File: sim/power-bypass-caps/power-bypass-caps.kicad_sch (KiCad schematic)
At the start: 248 parts

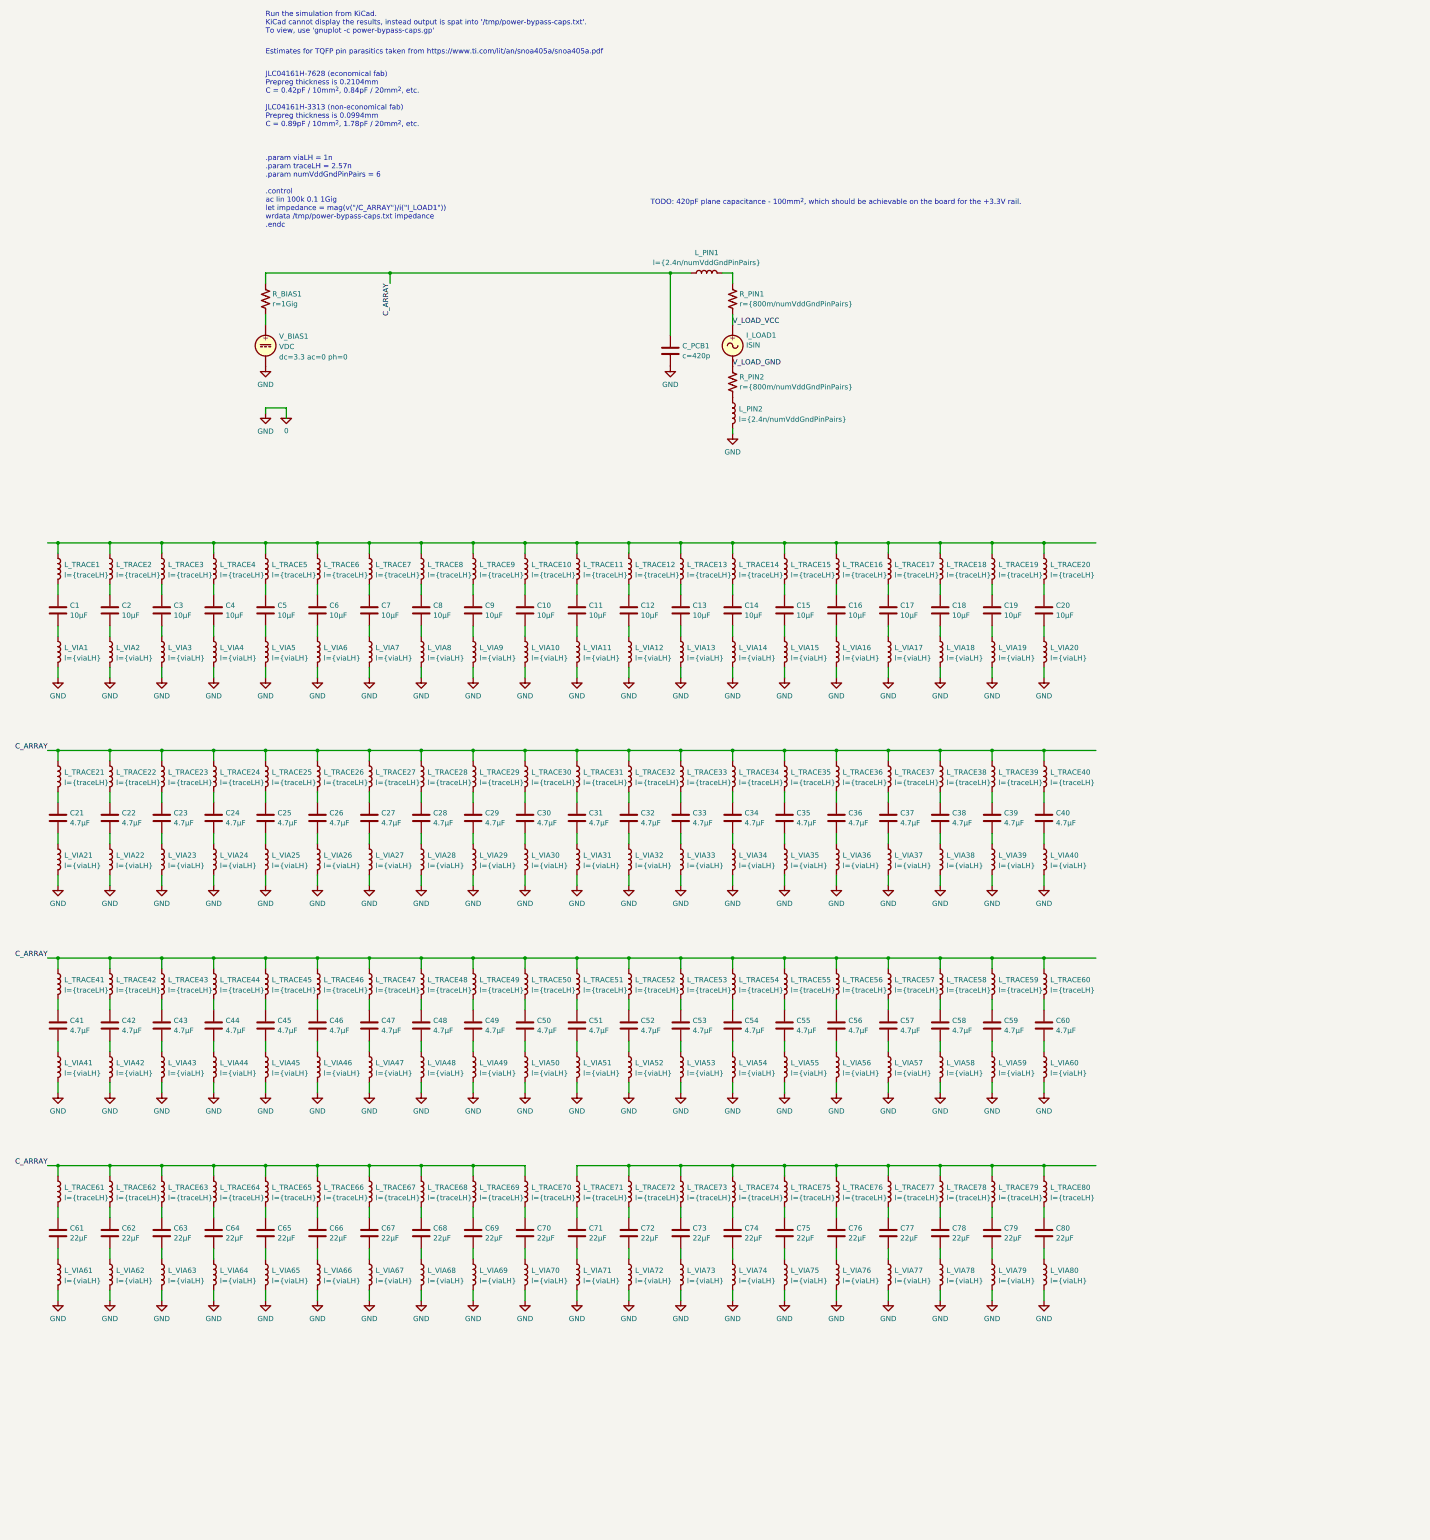
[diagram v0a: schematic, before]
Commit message: Some simulations around bypass capacitors.
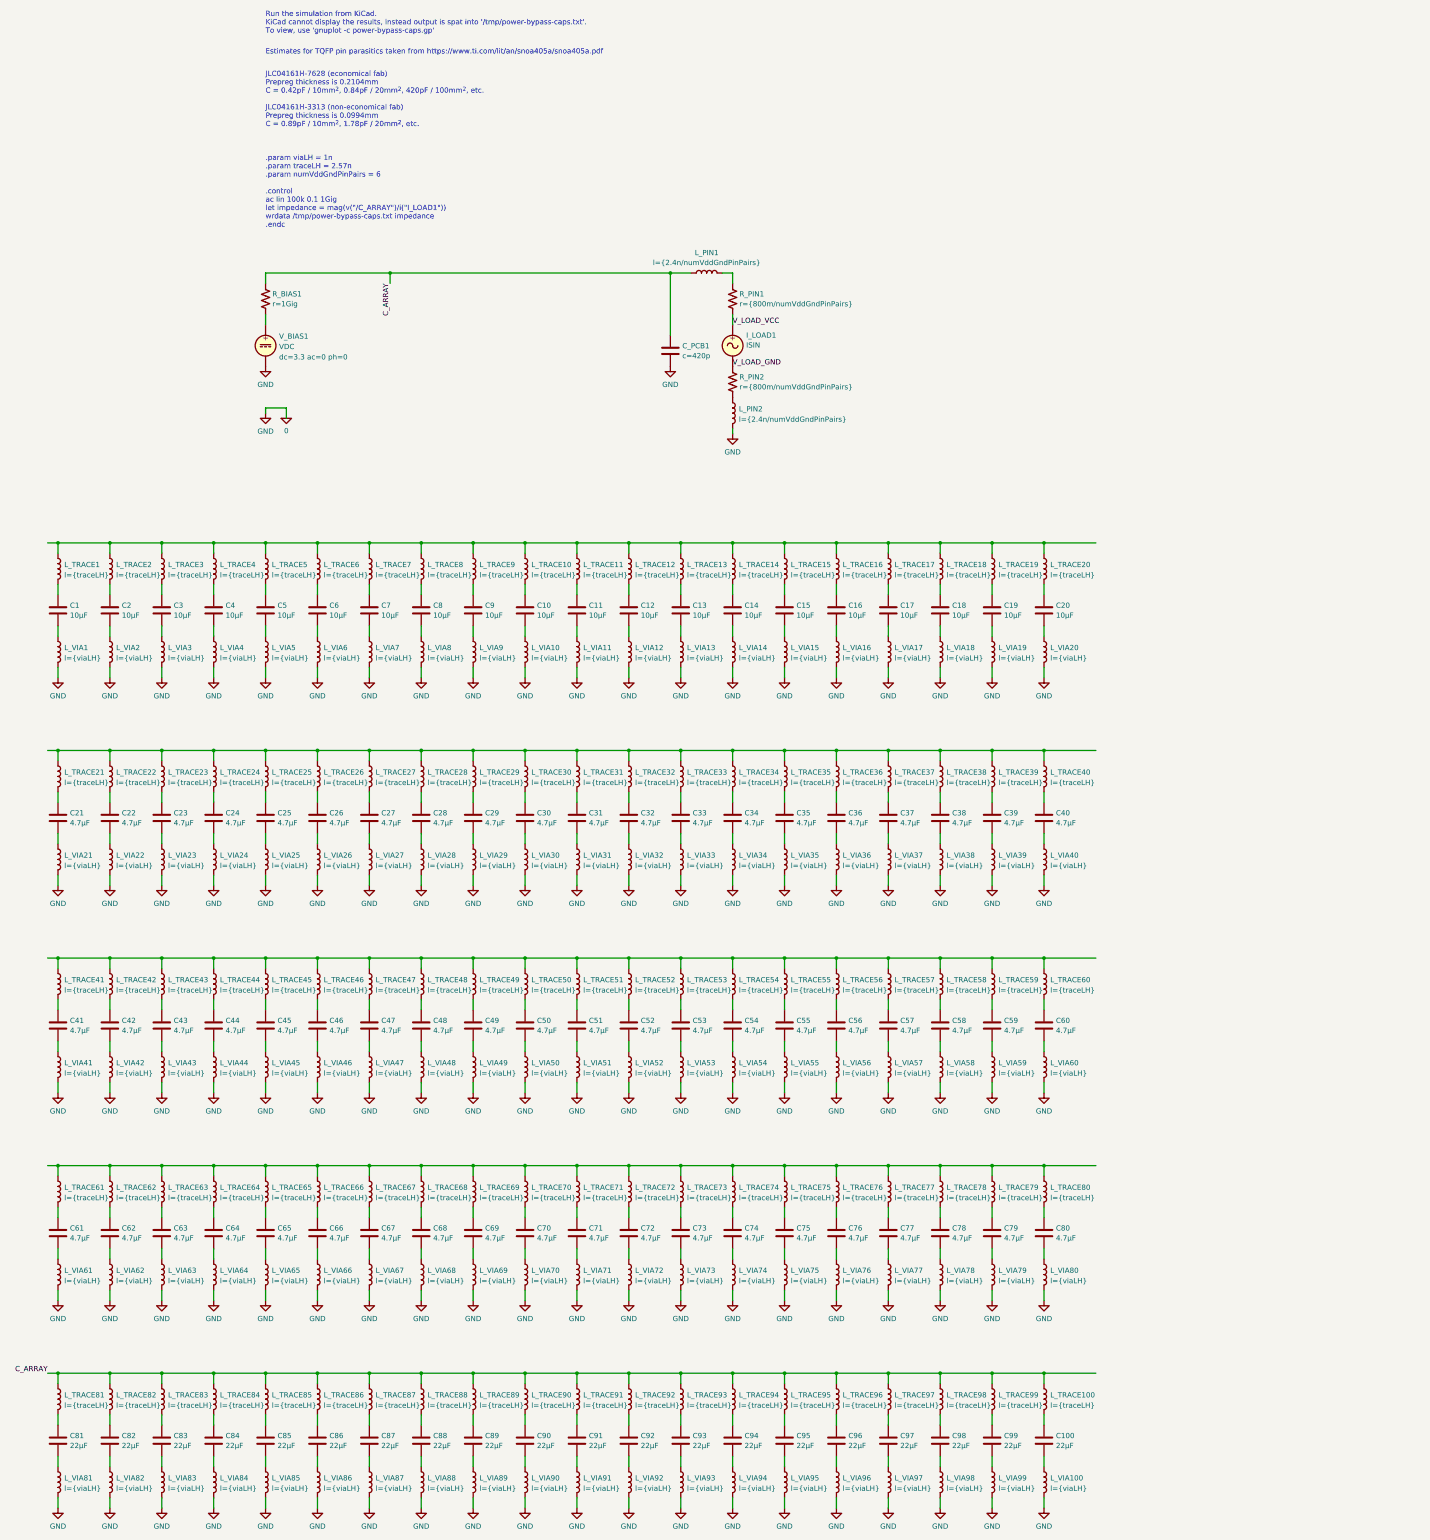
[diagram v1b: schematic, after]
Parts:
- added C100, C81, C82, C83, C84, C85, C86, C87, C88, C89, C90, C91, C92, C93, C94, C95, C96, C97, C98, C99: 22μF, restall-generic-capacitors:unpolarised-nominal-0402-1005, symbol restall-generic-capacitors:capacitor-unpolarised
- added L_TRACE100, L_TRACE81, L_TRACE82, L_TRACE83, L_TRACE84, L_TRACE85, L_TRACE86, L_TRACE87, L_TRACE88, L_TRACE89, L_TRACE90, L_TRACE91, L_TRACE92, L_TRACE93, L_TRACE94, L_TRACE95, L_TRACE96, L_TRACE97, L_TRACE98, L_TRACE99, L_VIA100, L_VIA81, L_VIA82, L_VIA83, L_VIA84, L_VIA85, L_VIA86, L_VIA87, L_VIA88, L_VIA89, L_VIA90, L_VIA91, L_VIA92, L_VIA93, L_VIA94, L_VIA95, L_VIA96, L_VIA97, L_VIA98, L_VIA99: ${SIM.PARAMS}, symbol restall-generic-inductors:l-air
- C61, C62, C63, C64, C65, C66, C67, C68, C69, C70, C71, C72, C73, C74, C75, C76, C77, C78, C79, C80: value 22μF -> 4.7μF
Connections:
- net 0: now also L_VIA100.2 (P2), L_VIA81.2 (P2), L_VIA82.2 (P2), L_VIA83.2 (P2), L_VIA84.2 (P2), L_VIA85.2 (P2), L_VIA86.2 (P2), L_VIA87.2 (P2), L_VIA88.2 (P2), L_VIA89.2 (P2), L_VIA90.2 (P2), L_VIA91.2 (P2), L_VIA92.2 (P2), L_VIA93.2 (P2), L_VIA94.2 (P2), L_VIA95.2 (P2), L_VIA96.2 (P2), L_VIA97.2 (P2), L_VIA98.2 (P2), L_VIA99.2 (P2)
- net C_ARRAY: now also L_TRACE100.1 (P1), L_TRACE81.1 (P1), L_TRACE82.1 (P1), L_TRACE83.1 (P1), L_TRACE84.1 (P1), L_TRACE85.1 (P1), L_TRACE86.1 (P1), L_TRACE87.1 (P1), L_TRACE88.1 (P1), L_TRACE89.1 (P1), L_TRACE90.1 (P1), L_TRACE91.1 (P1), L_TRACE92.1 (P1), L_TRACE93.1 (P1), L_TRACE94.1 (P1), L_TRACE95.1 (P1), L_TRACE96.1 (P1), L_TRACE97.1 (P1), L_TRACE98.1 (P1), L_TRACE99.1 (P1); no longer L_TRACE21.1 (P1), L_TRACE22.1 (P1), L_TRACE23.1 (P1), L_TRACE24.1 (P1), L_TRACE25.1 (P1), L_TRACE26.1 (P1), L_TRACE27.1 (P1), L_TRACE28.1 (P1), L_TRACE29.1 (P1), L_TRACE30.1 (P1), L_TRACE31.1 (P1), L_TRACE32.1 (P1), L_TRACE33.1 (P1), L_TRACE34.1 (P1), L_TRACE35.1 (P1), L_TRACE36.1 (P1), L_TRACE37.1 (P1), L_TRACE38.1 (P1), L_TRACE39.1 (P1), L_TRACE40.1 (P1), L_TRACE41.1 (P1), L_TRACE42.1 (P1), L_TRACE43.1 (P1), L_TRACE44.1 (P1), L_TRACE45.1 (P1), L_TRACE46.1 (P1), L_TRACE47.1 (P1), L_TRACE48.1 (P1), L_TRACE49.1 (P1), L_TRACE50.1 (P1), L_TRACE51.1 (P1), L_TRACE52.1 (P1), L_TRACE53.1 (P1), L_TRACE54.1 (P1), L_TRACE55.1 (P1), L_TRACE56.1 (P1), L_TRACE57.1 (P1), L_TRACE58.1 (P1), L_TRACE59.1 (P1), L_TRACE60.1 (P1), L_TRACE61.1 (P1), L_TRACE62.1 (P1), L_TRACE63.1 (P1), L_TRACE64.1 (P1), L_TRACE65.1 (P1), L_TRACE66.1 (P1), L_TRACE67.1 (P1), L_TRACE68.1 (P1), L_TRACE69.1 (P1), L_TRACE70.1 (P1)
- net at L_TRACE71.1 (P1), L_TRACE72.1 (P1), L_TRACE73.1 (P1)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: now also L_TRACE61.1 (P1), L_TRACE62.1 (P1), L_TRACE63.1 (P1), L_TRACE64.1 (P1), L_TRACE65.1 (P1), L_TRACE66.1 (P1), L_TRACE67.1 (P1), L_TRACE68.1 (P1), L_TRACE69.1 (P1), L_TRACE70.1 (P1)
- new net: C99.1, L_TRACE99.2 (P2)
- new net: C99.2, L_VIA99.1 (P1)
- new net: C94.1, L_TRACE94.2 (P2)
- new net: C94.2, L_VIA94.1 (P1)
- new net: C97.1, L_TRACE97.2 (P2)
- new net: L_TRACE21.1 (P1), L_TRACE22.1 (P1), L_TRACE23.1 (P1), L_TRACE24.1 (P1), L_TRACE25.1 (P1), L_TRACE26.1 (P1), L_TRACE27.1 (P1), L_TRACE28.1 (P1), L_TRACE29.1 (P1), L_TRACE30.1 (P1), L_TRACE31.1 (P1), L_TRACE32.1 (P1), L_TRACE33.1 (P1), L_TRACE34.1 (P1), L_TRACE35.1 (P1), L_TRACE36.1 (P1), L_TRACE37.1 (P1), L_TRACE38.1 (P1), L_TRACE39.1 (P1), L_TRACE40.1 (P1)
- new net: C90.1, L_TRACE90.2 (P2)
- new net: C90.2, L_VIA90.1 (P1)
- new net: L_TRACE41.1 (P1), L_TRACE42.1 (P1), L_TRACE43.1 (P1), L_TRACE44.1 (P1), L_TRACE45.1 (P1), L_TRACE46.1 (P1), L_TRACE47.1 (P1), L_TRACE48.1 (P1), L_TRACE49.1 (P1), L_TRACE50.1 (P1), L_TRACE51.1 (P1), L_TRACE52.1 (P1), L_TRACE53.1 (P1), L_TRACE54.1 (P1), L_TRACE55.1 (P1), L_TRACE56.1 (P1), L_TRACE57.1 (P1), L_TRACE58.1 (P1), L_TRACE59.1 (P1), L_TRACE60.1 (P1)
- new net: C82.2, L_VIA82.1 (P1)
- new net: C81.1, L_TRACE81.2 (P2)
- new net: C81.2, L_VIA81.1 (P1)
- new net: C98.1, L_TRACE98.2 (P2)
- new net: C86.1, L_TRACE86.2 (P2)
- new net: C98.2, L_VIA98.1 (P1)
- new net: C87.1, L_TRACE87.2 (P2)
- new net: C91.2, L_VIA91.1 (P1)
- new net: C85.1, L_TRACE85.2 (P2)
- new net: C85.2, L_VIA85.1 (P1)
- new net: C89.1, L_TRACE89.2 (P2)
- new net: C96.1, L_TRACE96.2 (P2)
- new net: C96.2, L_VIA96.1 (P1)
- new net: C97.2, L_VIA97.1 (P1)
- new net: C83.1, L_TRACE83.2 (P2)
- new net: C83.2, L_VIA83.1 (P1)
- new net: C88.1, L_TRACE88.2 (P2)
- new net: C82.1, L_TRACE82.2 (P2)
- new net: C92.1, L_TRACE92.2 (P2)
- new net: C92.2, L_VIA92.1 (P1)
- new net: C93.1, L_TRACE93.2 (P2)
- new net: C93.2, L_VIA93.1 (P1)
- new net: C95.2, L_VIA95.1 (P1)
- new net: C100.1, L_TRACE100.2 (P2)
- new net: C87.2, L_VIA87.1 (P1)
- new net: C100.2, L_VIA100.1 (P1)
- new net: C89.2, L_VIA89.1 (P1)
- new net: C86.2, L_VIA86.1 (P1)
- new net: C95.1, L_TRACE95.2 (P2)
- new net: C84.2, L_VIA84.1 (P1)
- new net: C91.1, L_TRACE91.2 (P2)
- new net: C88.2, L_VIA88.1 (P1)
- new net: C84.1, L_TRACE84.2 (P2)
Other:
- note added: "JLC04161H-7628 (economical fab) Prepreg thickness is 0.2104mm C = 0.42pF / 10mm^{2}, 0.84pF / 20mm^{2}, 420pF / 100mm^{2}, etc. JLC04161H-3313 (non-economical fab) Prepreg thickness is 0.0994mm C = 0.89pF / 10mm^{2}, 1.78pF / 20mm^{2}, etc."
- note removed: "JLC04161H-7628 (economical fab) Prepreg thickness is 0.2104mm C = 0.42pF / 10mm^{2}, 0.84pF / 20mm^{2}, etc. JLC04161H-3313 (non-economical fab) Prepreg thickness is 0.0994mm C = 0.89pF / 10mm^{2}, 1.78pF / 20mm^{2}, etc."
- note removed: "TODO: 420pF plane capacitance - 100mm^{2}, which should be achievable on the board for the +3.3V rail."

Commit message: Initial stab at a simulation for the buck regulator.  Started to flesh out the USB / power schematics.  More work required to figure out the large ripple on the buck regulator's input, which looks to be related to the ESL of the input capacitors.
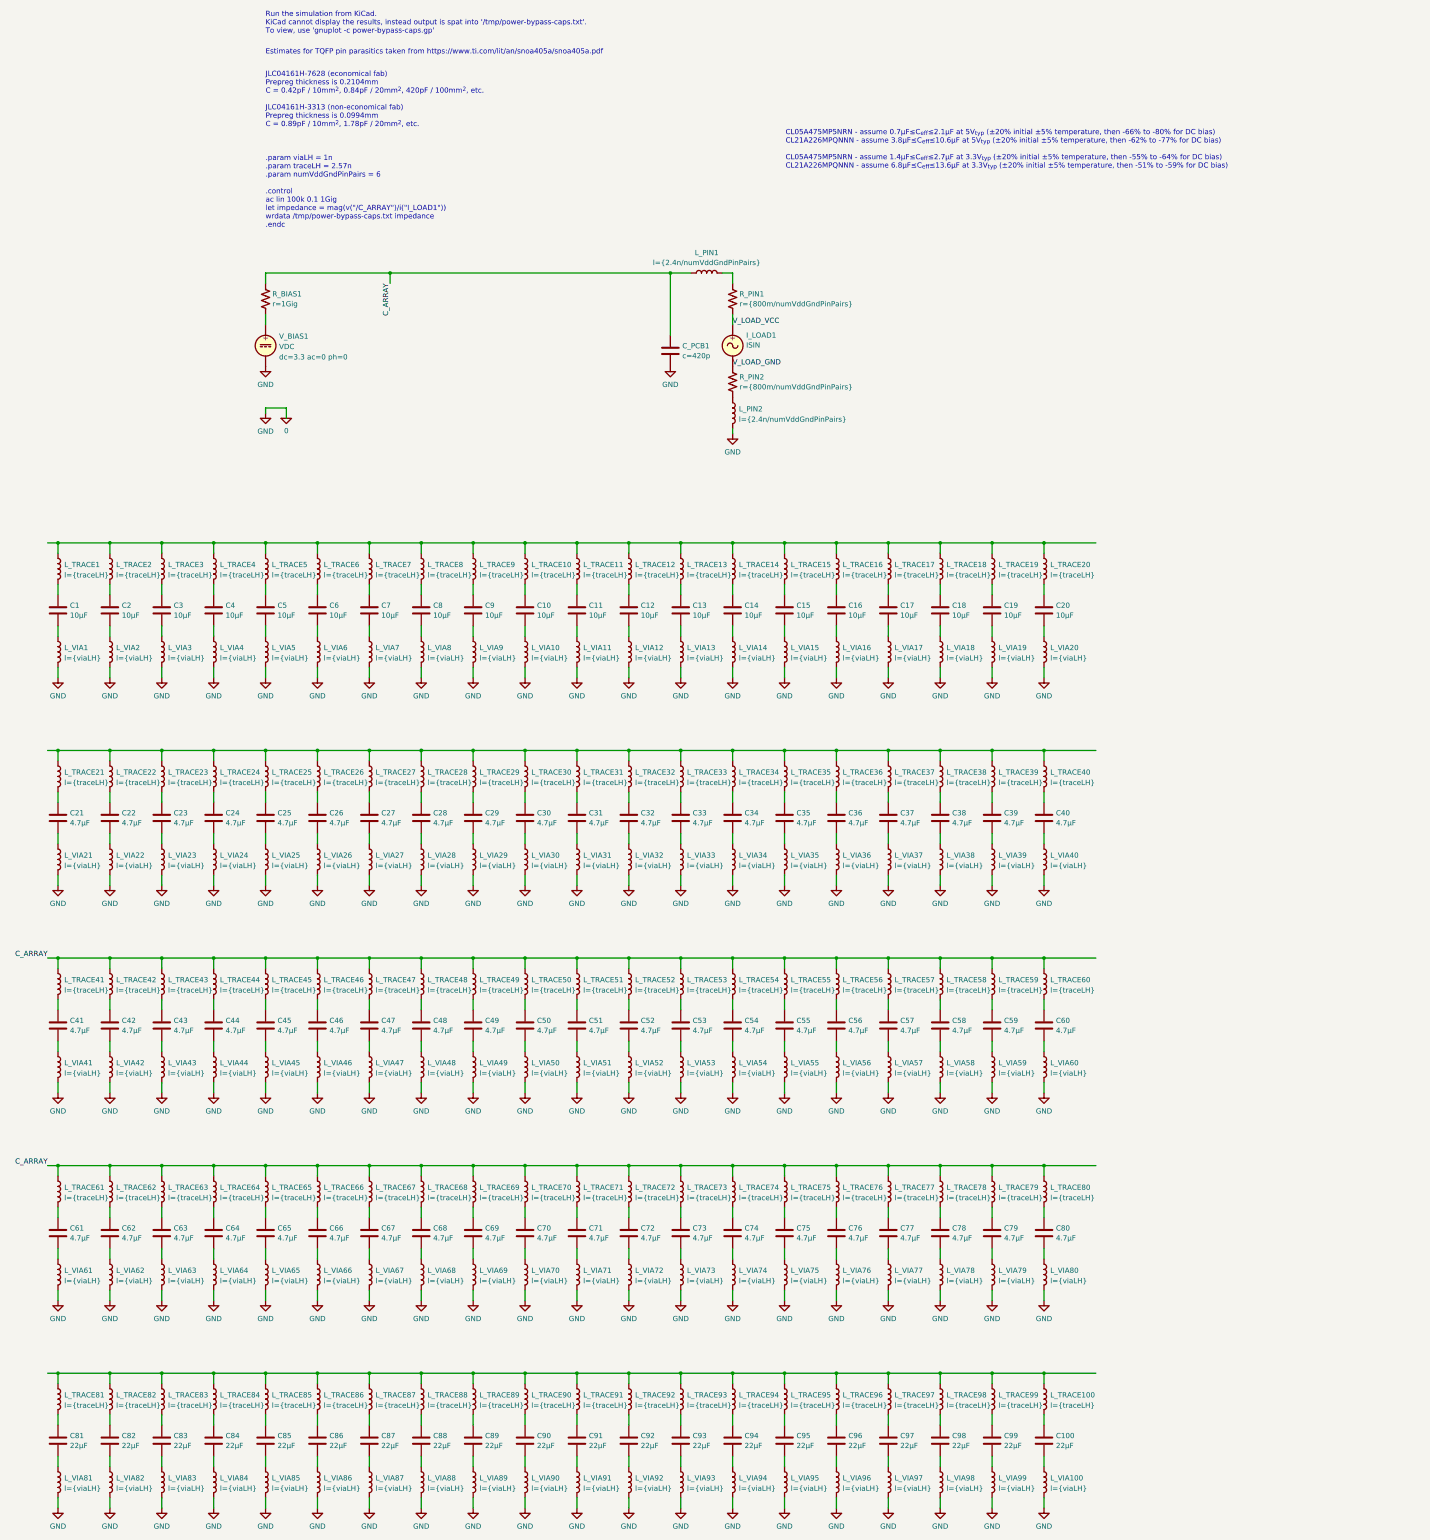
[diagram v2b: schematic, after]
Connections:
- net C_ARRAY: now also L_TRACE41.1 (P1), L_TRACE42.1 (P1), L_TRACE43.1 (P1), L_TRACE44.1 (P1), L_TRACE45.1 (P1), L_TRACE46.1 (P1), L_TRACE47.1 (P1), L_TRACE48.1 (P1), L_TRACE49.1 (P1), L_TRACE50.1 (P1), L_TRACE51.1 (P1), L_TRACE52.1 (P1), L_TRACE53.1 (P1), L_TRACE54.1 (P1), L_TRACE55.1 (P1), L_TRACE56.1 (P1), L_TRACE57.1 (P1), L_TRACE58.1 (P1), L_TRACE59.1 (P1), L_TRACE60.1 (P1), L_TRACE61.1 (P1), L_TRACE62.1 (P1), L_TRACE63.1 (P1), L_TRACE64.1 (P1), L_TRACE65.1 (P1), L_TRACE66.1 (P1), L_TRACE67.1 (P1), L_TRACE68.1 (P1), L_TRACE69.1 (P1), L_TRACE70.1 (P1), L_TRACE71.1 (P1), L_TRACE72.1 (P1), L_TRACE73.1 (P1), L_TRACE74.1 (P1), L_TRACE75.1 (P1), L_TRACE76.1 (P1), L_TRACE77.1 (P1), L_TRACE78.1 (P1), L_TRACE79.1 (P1), L_TRACE80.1 (P1); no longer L_TRACE100.1 (P1), L_TRACE81.1 (P1), L_TRACE82.1 (P1), L_TRACE83.1 (P1), L_TRACE84.1 (P1), L_TRACE85.1 (P1), L_TRACE86.1 (P1), L_TRACE87.1 (P1), L_TRACE88.1 (P1), L_TRACE89.1 (P1), L_TRACE90.1 (P1), L_TRACE91.1 (P1), L_TRACE92.1 (P1), L_TRACE93.1 (P1), L_TRACE94.1 (P1), L_TRACE95.1 (P1), L_TRACE96.1 (P1), L_TRACE97.1 (P1), L_TRACE98.1 (P1), L_TRACE99.1 (P1)
- new net: L_TRACE100.1 (P1), L_TRACE81.1 (P1), L_TRACE82.1 (P1), L_TRACE83.1 (P1), L_TRACE84.1 (P1), L_TRACE85.1 (P1), L_TRACE86.1 (P1), L_TRACE87.1 (P1), L_TRACE88.1 (P1), L_TRACE89.1 (P1), L_TRACE90.1 (P1), L_TRACE91.1 (P1), L_TRACE92.1 (P1), L_TRACE93.1 (P1), L_TRACE94.1 (P1), L_TRACE95.1 (P1), L_TRACE96.1 (P1), L_TRACE97.1 (P1), L_TRACE98.1 (P1), L_TRACE99.1 (P1)
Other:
- note added: "CL05A475MP5NRN - assume 0.7μF≤C_{eff}≤2.1μF at 5V_{typ} (±20% initial ±5% temperature, then -66% to -80% for DC bias) CL21A226MPQNNN - assume 3.8μF≤C_{eff}≤10.6μF at 5V_{typ} (±20% initial ±5% temperature, then -62% to -77% for DC bias) CL05A475MP5NRN - assume 1.4μF≤C_{eff}≤2.7μF at 3.3V_{typ} (±20% initial ±5% temperature, then -55% to -64% for DC bias) CL21A226MPQNNN - assume 6.8μF≤C_{eff}≤13.6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"
